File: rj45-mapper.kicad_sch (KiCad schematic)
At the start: 34 parts, among them J1 RC01937, J2 USB-C_5V, Q1 MMBT3904, U1 ULN2803A

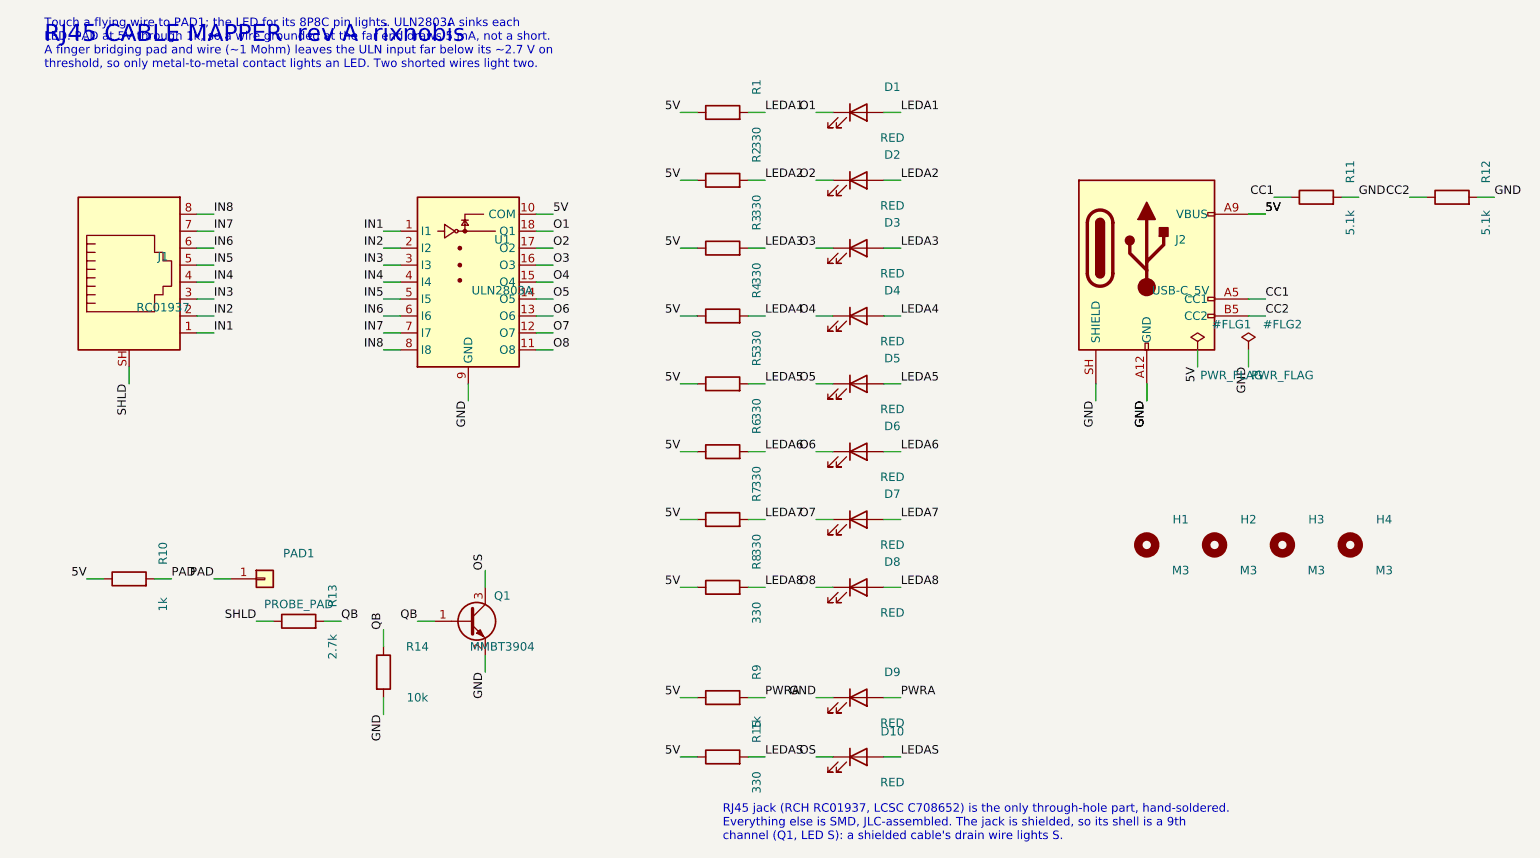
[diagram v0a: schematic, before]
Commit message: Rev A2: right-angle jack on the 8P8C drawing, plug-path check
The RC01937 is a top-entry jack, so the case wall faced a closed side. J1 is now
an unshielded right-angle jack on the TE 5555164 / Amphenol 54602 land pattern
(0.89 mm pins, 3.25 mm pegs), bought separately, with its plug face flush with
the board edge; the TE model is aligned to the pads and the face. The shield
channel is gone. fit_check.py now casts rays along the plug path from outside
the case into the jack.
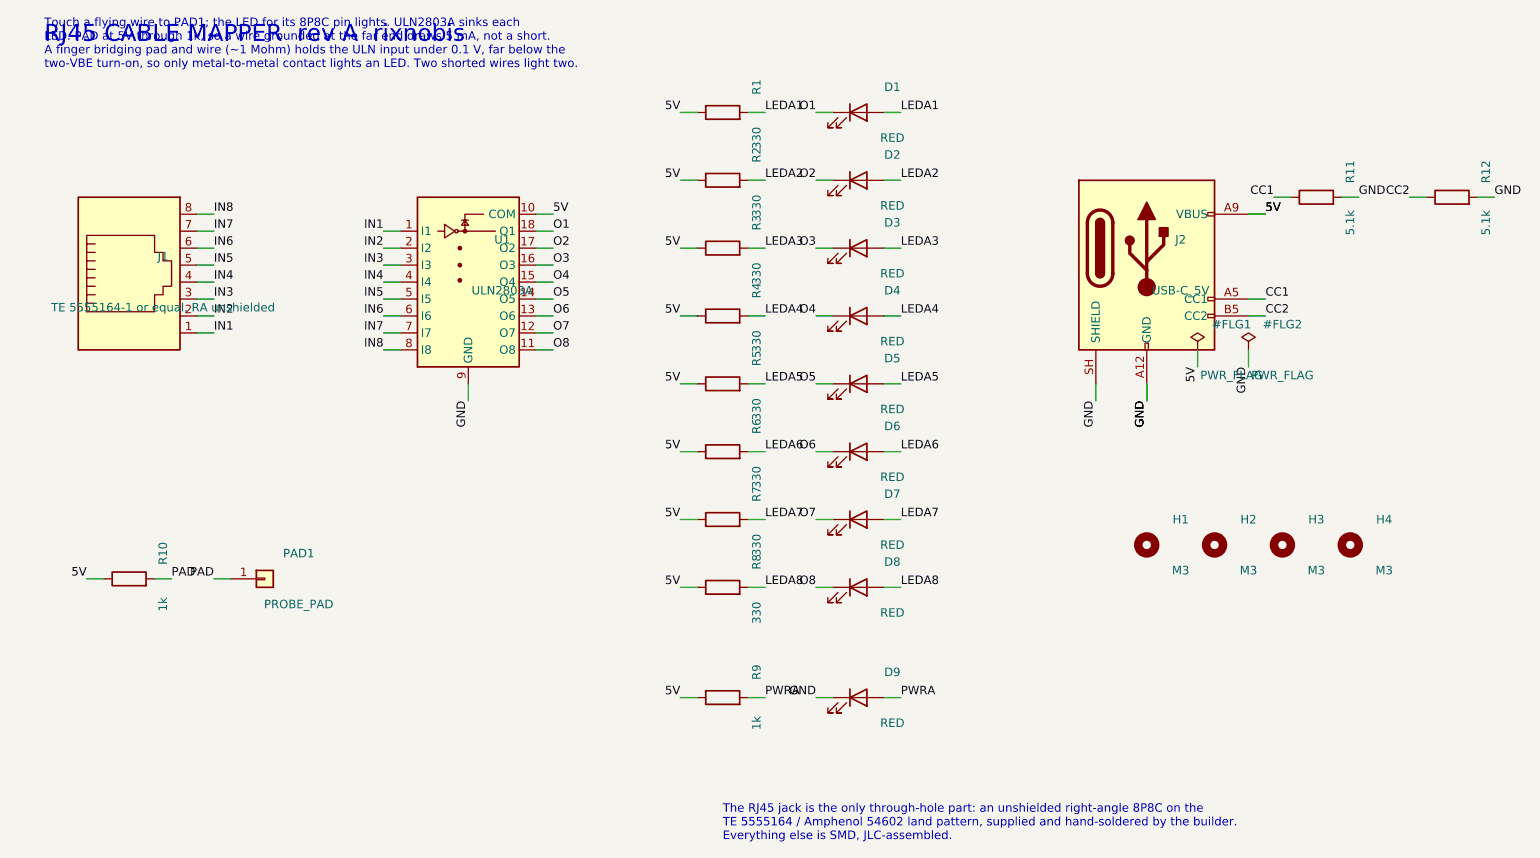
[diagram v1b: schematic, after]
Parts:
- removed D10: RED, LED_SMD:LED_1206_3216Metric, symbol Device:LED
- removed J1: RC01937, rj45-mapper:RJ45_RCH_RC01937, symbol Connector:8P8C_Shielded
- removed Q1: MMBT3904, Package_TO_SOT_SMD:SOT-23, symbol Transistor_BJT:Q_NPN_BEC
- removed R13: 2.7k, Resistor_SMD:R_0805_2012Metric, symbol Device:R
- removed R14: 10k, Resistor_SMD:R_0805_2012Metric, symbol Device:R
- removed R15: 330, Resistor_SMD:R_0805_2012Metric, symbol Device:R
- added J1: TE 5555164-1 or equal, RA unshielded, rj45-mapper:RJ45_8P8C_RightAngle, symbol Connector:8P8C
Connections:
- net IN1: now also J1.1
- net IN2: now also J1.2
- net IN3: now also J1.3
- net IN4: now also J1.4
- net IN5: now also J1.5
- net IN6: now also J1.6
- net IN7: now also J1.7
- net IN8: now also J1.8
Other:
- note added: "The RJ45 jack is the only through-hole part: an unshielded right-angle 8P8C on the TE 5555164 / Amphenol 54602 land pattern, supplied and hand-soldered by the builder. Everything else is SMD, JLC-assembled."
- note added: "Touch a flying wire to PAD1; the LED for its 8P8C pin lights. ULN2803A sinks each LED. PAD at 5V through 1k, so a wire grounded at the far end draws 5 mA, not a short. A finger bridging pad and wire (~1 Mohm) holds the ULN input under 0.1 V, far below the two-VBE turn-on, so only metal-to-metal contact lights an LED. Two shorted wires light two."
- note removed: "RJ45 jack (RCH RC01937, LCSC C708652) is the only through-hole part, hand-soldered. Everything else is SMD, JLC-assembled. The jack is shielded, so its shell is a 9th channel (Q1, LED S): a shielded cable's drain wire lights S."
- note removed: "Touch a flying wire to PAD1; the LED for its 8P8C pin lights. ULN2803A sinks each LED. PAD at 5V through 1k, so a wire grounded at the far end draws 5 mA, not a short. A finger bridging pad and wire (~1 Mohm) leaves the ULN input far below its ~2.7 V on threshold, so only metal-to-metal contact lights an LED. Two shorted wires light two."
